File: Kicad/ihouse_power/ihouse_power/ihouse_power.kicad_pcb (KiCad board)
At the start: 2 copper layers, 212 x 156 mm, 203 parts, among them J1 Conn_02x12_Top_Bottom, J10 Conn_02x07_Odd_Even, J11 Conn_01x06, J13 RJ33_Shielded, J14 Optic, J15 Hum1, J16 Hum2, J17 Hum3, J18 Temp, J19 I2C, J2 Conn_02x05_Top_Bottom, J20 Conn_02x05_Top_Bottom, J21 RS232, J22 Nextion, J3 Conn_01x20, J4 Conn_01x20, J5 Conn_01x16, J6 Conn_01x06, J7 Conn_02x07_Odd_Even, J8 Conn_01x16, J9 Conn_01x06, K1 FINDER-34.51, K10 FINDER-34.51, K11 FINDER-34.51, K12 FINDER-34.51, K13 FINDER-34.51, K14 FINDER-41.52, K2 FINDER-34.51, K3 FINDER-34.51, K4 FINDER-34.51, K5 FINDER-34.51, K6 FINDER-34.51, K7 FINDER-34.51, K8 FINDER-34.51, K9 FINDER-34.51, M1 stm32f1_module, M2 tb387_uart_expander, M3 ev1527receiver_module, Q1 IRF7403, Q2 IRF7403, Q3 IRF7403, Q4 IRF7403, Q5 BC847, U1 ULN2004, U10 MAX232, U11 L7805, U12 MAX232, U2 ULN2004, U3 L293D, U4 MCP23017_SO, U5 L7805, U6 EL814, U7 EL814, U8 EL814, U9 24LC32

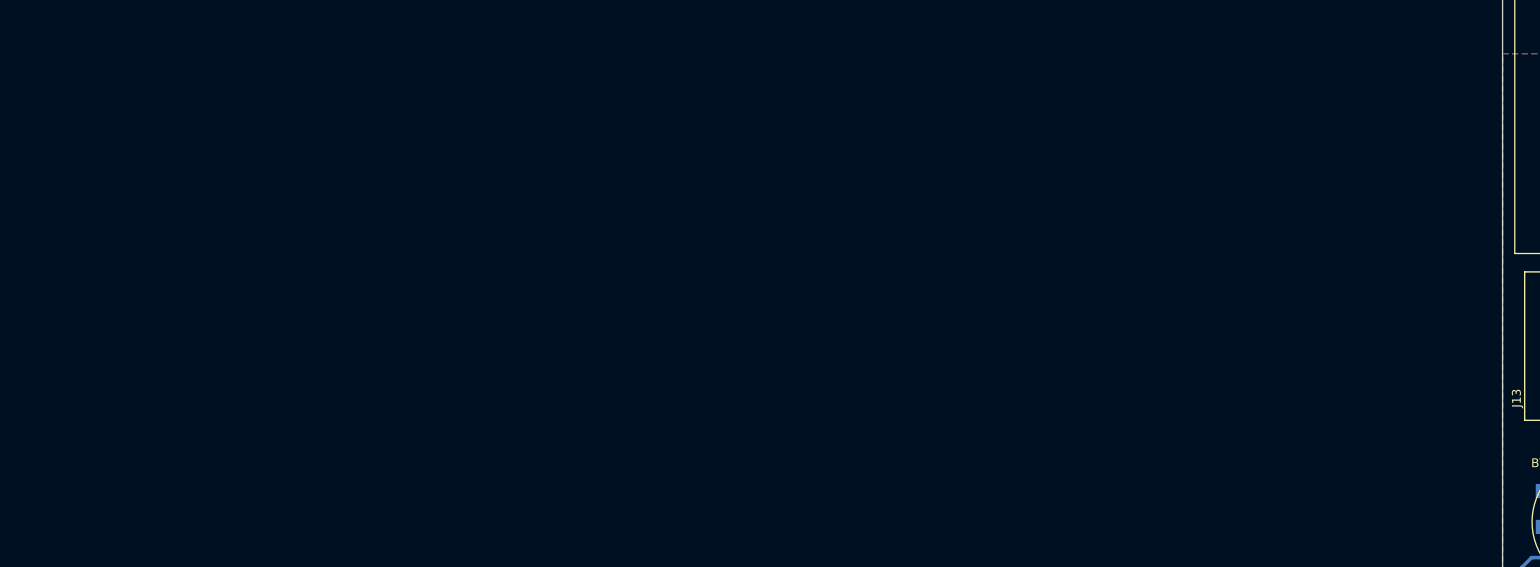
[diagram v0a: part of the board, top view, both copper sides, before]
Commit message: nupiesta paskirstymo dezutes schema ir pcb
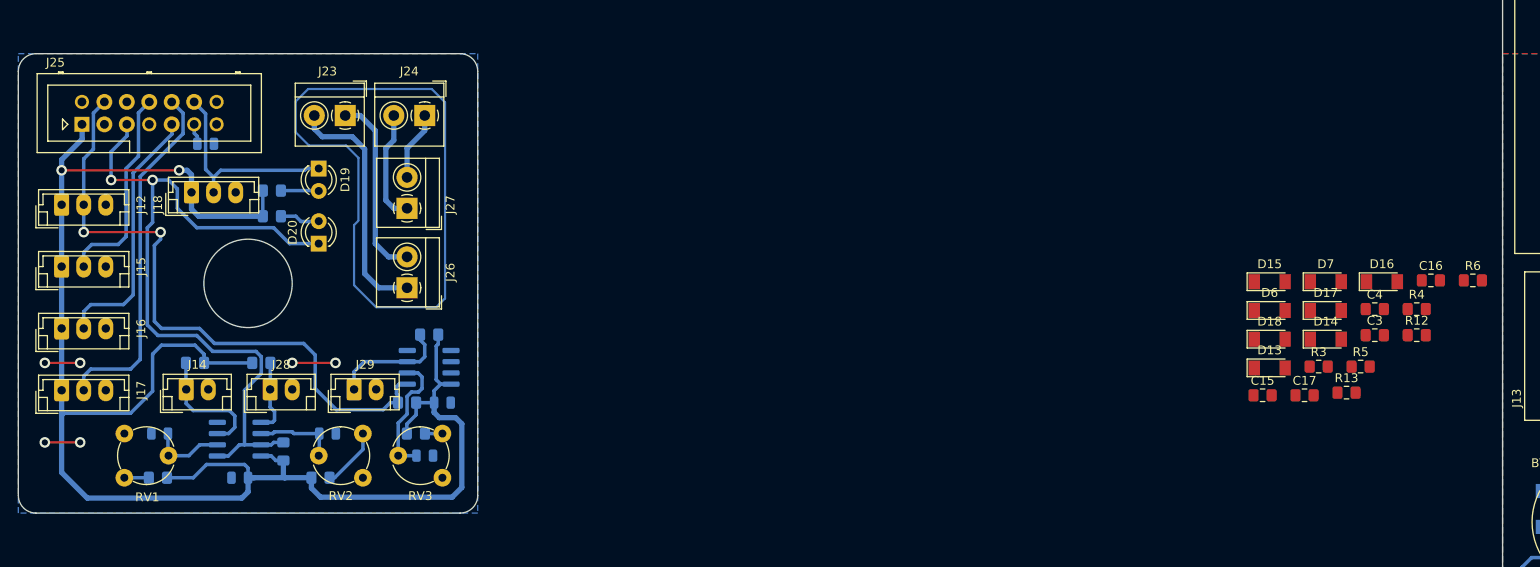
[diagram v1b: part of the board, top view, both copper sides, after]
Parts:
- added C15: 0.1, Capacitor_SMD:C_0805_2012Metric_Pad1.15x1.40mm_HandSolder, F.Cu at (19.8, 94.7)
- added C16: 0.1, Capacitor_SMD:C_0805_2012Metric_Pad1.15x1.40mm_HandSolder, F.Cu at (38.9, 81.7)
- added C17: 0.1, Capacitor_SMD:C_0805_2012Metric_Pad1.15x1.40mm_HandSolder, F.Cu at (24.6, 94.7)
- added C21: 0.1, Capacitor_SMD:C_0805_2012Metric, B.Cu at (-95.9, 104.0)
- added C3: 0.1, Capacitor_SMD:C_0805_2012Metric_Pad1.15x1.40mm_HandSolder, F.Cu at (32.5, 87.9)
- added C35: 0.1, Capacitor_SMD:C_0805_2012Metric, B.Cu at (-105.0, 99.0)
- added C36: 0.1, Capacitor_SMD:C_0805_2012Metric, B.Cu at (-86.0, 99.0)
- added C37: 0.1, Capacitor_SMD:C_0805_2012Metric, B.Cu at (-73.0, 95.5)
- added C38: 0.1, Capacitor_SMD:C_0805_2012Metric, B.Cu at (-75.0, 101.5)
- added C4: 0.1, Capacitor_SMD:C_0805_2012Metric_Pad1.15x1.40mm_HandSolder, F.Cu at (32.5, 84.9)
- added D13: BAS32, Diode_SMD:D_MiniMELF, F.Cu at (20.6, 91.6)
- added D14: BAS32, Diode_SMD:D_MiniMELF, F.Cu at (27.0, 88.3)
- added D15: BAS32, Diode_SMD:D_MiniMELF, F.Cu at (20.6, 81.8)
- added D16: BAS32, Diode_SMD:D_MiniMELF, F.Cu at (33.3, 81.8)
- added D17: BAS85, Diode_SMD:D_MiniMELF, F.Cu at (27.0, 85.1)
- added D18: D, Diode_SMD:D_MiniMELF, F.Cu at (20.6, 88.3)
- added D19: DTH LINK, LED_THT:LED_D3.0mm, F.Cu at (-87.0, 69.0)
- added D20: PHOTO, LED_THT:LED_D3.0mm, F.Cu at (-87.0, 77.5)
- added D6: BAS32, Diode_SMD:D_MiniMELF, F.Cu at (20.6, 85.1)
- added D7: BAS32, Diode_SMD:D_MiniMELF, F.Cu at (27.0, 81.8)
- added J12: OPTIC, Connector_JST:JST_EH_B3B-EH-A_1x03_P2.50mm_Vertical, F.Cu at (-116.1, 73.1)
- added J14: OPT1, Connector_JST:JST_EH_B2B-EH-A_1x02_P2.50mm_Vertical, F.Cu at (-102.0, 94.0)
- added J15: LEAK1, Connector_JST:JST_EH_B3B-EH-A_1x03_P2.50mm_Vertical, F.Cu at (-116.1, 80.1)
- added J16: LEAK2, Connector_JST:JST_EH_B3B-EH-A_1x03_P2.50mm_Vertical, F.Cu at (-116.1, 87.1)
- added J17: LEAK3, Connector_JST:JST_EH_B3B-EH-A_1x03_P2.50mm_Vertical, F.Cu at (-116.1, 94.1)
- added J18: DHT22, Connector_JST:JST_EH_B3B-EH-A_1x03_P2.50mm_Vertical, F.Cu at (-101.4, 71.7)
- added J23: Valve1, TerminalBlock_4Ucon:TerminalBlock_4Ucon_1x02_P3.50mm_Horizontal, F.Cu at (-84.0, 63.0)
- added J24: Valve2, TerminalBlock_4Ucon:TerminalBlock_4Ucon_1x02_P3.50mm_Horizontal, F.Cu at (-75.0, 63.0)
- added J25: Conn_01x14, Connector_Multicomp:Multicomp_MC9A12-1434_2x07_P2.54mm_Vertical, F.Cu at (-113.8, 64.0)
- added J26: Valve1, TerminalBlock_4Ucon:TerminalBlock_4Ucon_1x02_P3.50mm_Horizontal, F.Cu at (-77.0, 82.5)
- added J27: Valve2, TerminalBlock_4Ucon:TerminalBlock_4Ucon_1x02_P3.50mm_Horizontal, F.Cu at (-77.0, 73.5)
- added J28: OPT2, Connector_JST:JST_EH_B2B-EH-A_1x02_P2.50mm_Vertical, F.Cu at (-92.5, 94.0)
- added J29: OPT3, Connector_JST:JST_EH_B2B-EH-A_1x02_P2.50mm_Vertical, F.Cu at (-83.0, 94.0)
- added R12: 100, Resistor_SMD:R_0805_2012Metric_Pad1.15x1.40mm_HandSolder, F.Cu at (37.3, 87.9)
- added R13: 47k, Resistor_SMD:R_0805_2012Metric_Pad1.15x1.40mm_HandSolder, F.Cu at (29.3, 94.4)
- added R14: 4.7k, Resistor_SMD:R_0805_2012Metric_Pad1.15x1.40mm_HandSolder, B.Cu at (-92.3, 71.5)
- added R15: R, Resistor_SMD:R_0805_2012Metric_Pad1.15x1.40mm_HandSolder, B.Cu at (-101.0, 91.0)
- added R17: 100, Resistor_SMD:R_0805_2012Metric_Pad1.15x1.40mm_HandSolder, B.Cu at (-105.2, 104.0)
- added R18: R, Resistor_SMD:R_0805_2012Metric_Pad1.15x1.40mm_HandSolder, B.Cu at (-93.5, 91.0)
- added R19: 100, Resistor_SMD:R_0805_2012Metric_Pad1.15x1.40mm_HandSolder, B.Cu at (-86.8, 104.0)
- added R20: 4.7k, Resistor_SMD:R_0805_2012Metric_Pad1.15x1.40mm_HandSolder, B.Cu at (-92.3, 74.4)
- added R24: R, Resistor_SMD:R_0805_2012Metric_Pad1.15x1.40mm_HandSolder, B.Cu at (-74.5, 87.8)
- added R25: 10k, Resistor_SMD:R_0805_2012Metric_Pad1.15x1.40mm_HandSolder, B.Cu at (-91.0, 101.0)
- added R26: 100, Resistor_SMD:R_0805_2012Metric_Pad1.15x1.40mm_HandSolder, B.Cu at (-76.0, 99.0)
- added R27: 10k, Resistor_SMD:R_0805_2012Metric_Pad1.15x1.40mm_HandSolder, B.Cu at (-77.0, 95.5)
- added R3: 100, Resistor_SMD:R_0805_2012Metric_Pad1.15x1.40mm_HandSolder, F.Cu at (26.2, 91.4)
- added R4: 100, Resistor_SMD:R_0805_2012Metric_Pad1.15x1.40mm_HandSolder, F.Cu at (37.3, 84.9)
- added R5: 100, Resistor_SMD:R_0805_2012Metric_Pad1.15x1.40mm_HandSolder, F.Cu at (30.9, 91.4)
- added R6: 100, Resistor_SMD:R_0805_2012Metric_Pad1.15x1.40mm_HandSolder, F.Cu at (43.6, 81.7)
- added REF**: R_0805_2012Metric, Resistor_SMD:R_0805_2012Metric, B.Cu at (-99.8, 66.2)
- added RV1: 5k, Potentiometer_THT:Potentiometer_Piher_PT-6-V_Vertical, F.Cu at (-109.0, 104.0)
- added RV2: 5k, Potentiometer_THT:Potentiometer_Piher_PT-6-V_Vertical, F.Cu at (-82.0, 99.0)
- added RV3: 5k, Potentiometer_THT:Potentiometer_Piher_PT-6-V_Vertical, F.Cu at (-73.0, 99.0)
- added U6: LM393, Package_SO:SOIC-8_3.9x4.9mm_P1.27mm, B.Cu at (-96.0, 99.6)
- added U7: LM393, Package_SO:SOIC-8_3.9x4.9mm_P1.27mm, B.Cu at (-74.5, 91.5)
- C12, C13, C14, C18, C19, C20: value C -> 0.1
- D10: value D -> BAS32
- R31: value 100 -> 47R
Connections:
- net /MCU plokste/A15 renamed /MCU plokste/PA15
- net /MCU plokste/A2 renamed /MCU plokste/PA2
- net /MCU plokste/A3 renamed /MCU plokste/PA3
- net /MCU plokste/A8 renamed /MCU plokste/PA8
- net /MCU plokste/C13 renamed /MCU plokste/PC13
- net /MCU plokste/C14 renamed /MCU plokste/PC14
- net /MCU plokste/C15 renamed /MCU plokste/PC15
- C12 pad 1: /MCU plokste/VDDA -> /MCU plokste/5VDDA
- C14 pad 1: /MCU plokste/OPTIC_AI -> /MCU plokste/PA6
- C18 pad 1: /MCU plokste/VDDA -> /MCU plokste/5VDDA
- C19 pad 1: /MCU plokste/VDDA -> /MCU plokste/5VDDA
- C20 pad 1: /MCU plokste/VDDA -> /MCU plokste/5VDDA
- C27 pad 1: /MCU plokste/A7 -> /MCU plokste/PA0
- C5 pad 1: /MCU plokste/LPULSE -> /MCU plokste/PB3
- D10 pad 2: /MCU plokste/A7 -> /MCU plokste/PA0
- J1 pad 11: /K2.11 -> /Reliu modulis/K2.11
- J1 pad 12: /K1.11 -> /Reliu modulis/K1.11
- J1 pad 23: /K2.14 -> /Reliu modulis/K2.14
- J1 pad 24: /K1.14 -> /Reliu modulis/K1.14
- J3 pad 10: /MCU plokste/LPULSE -> /MCU plokste/PB3
- J4 pad 10: /MCU plokste/A5 -> /MCU plokste/PA5
- J4 pad 11: /MCU plokste/A6 -> /MCU plokste/PA6
- J4 pad 12: /MCU plokste/A7 -> /MCU plokste/PA7
- J4 pad 15: /MCU plokste/LPULSE1 -> /MCU plokste/PB10
- J4 pad 16: /MCU plokste/LPULSE2 -> /MCU plokste/PB11
- J4 pad 5: /MCU plokste/A0 -> /MCU plokste/PA0
- J4 pad 6: /MCU plokste/A1 -> /MCU plokste/PA1
- J4 pad 9: /MCU plokste/A4 -> /MCU plokste/PA4
- K1 pad 11: /K1.11 -> /Reliu modulis/K1.11
- K1 pad 14: /K1.14 -> /Reliu modulis/K1.14
- K2 pad 11: /K2.11 -> /Reliu modulis/K2.11
- K2 pad 14: /K2.14 -> /Reliu modulis/K2.14
- M1 pad 10: /MCU plokste/HUM3_AI -> /MCU plokste/PA5
- M1 pad 11: /MCU plokste/TEMP_AI -> /MCU plokste/PA6
- M1 pad 12: /MCU plokste/A7 -> /MCU plokste/PA7
- M1 pad 15: /MCU plokste/LPULSE1 -> /MCU plokste/PB10
- M1 pad 16: /MCU plokste/LPULSE2 -> /MCU plokste/PB11
- M1 pad 30: /MCU plokste/LPULSE -> /MCU plokste/PB3
- M1 pad 5: /MCU plokste/OPTIC_AI -> /MCU plokste/PA0
- M1 pad 6: /MCU plokste/HUM1_AI -> /MCU plokste/PA1
- M1 pad 9: /MCU plokste/HUM2_AI -> /MCU plokste/PA4
- R10 pad 2: /MCU plokste/A7 -> /MCU plokste/PA0
- R11 pad 1: /MCU plokste/A7 -> /MCU plokste/PA0
- R2 pad 1: /MCU plokste/LPULSE -> Net-(D17-Pad2)
- R2 pad 2: /MCU plokste/5VDC -> /MCU plokste/3VDC
- R23 pad 1: /MCU plokste/OPTIC_AI -> /MCU plokste/PA6
- R23 pad 2: /MCU plokste/Optic -> /MCU plokste/OPTIC
- R31 pad 2: /MCU plokste/VDDA -> /MCU plokste/5VDDA
- R36 pad 1: /MCU plokste/230N -> /MCU plokste/230L
- R37 pad 1: /MCU plokste/230L -> /MCU plokste/230N
- U8 pad 4: /MCU plokste/LPULSE -> Net-(D17-Pad2)
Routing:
- net /Paskirstymo dezute/5VDC: track 0.00 -> 193.8 mm, vias 0 -> 2
- net /Paskirstymo dezute/OPTICWC: track 0.00 -> 84.7 mm, vias 0 -> 2
- net Net-(J507-Pad11): track 0.00 -> 78.4 mm
- net /Paskirstymo dezute/OPTIC: track 0.00 -> 72.3 mm, vias 0 -> 2
- net Net-(J17-Pad2): track 0.00 -> 40.5 mm
- net Net-(J16-Pad2): track 0.00 -> 29.4 mm
- net Net-(J23-Pad2): track 0.00 -> 27.7 mm
- net Net-(J15-Pad2): track 0.00 -> 23.5 mm
- net /Paskirstymo dezute/DATA: track 0.00 -> 23.5 mm
- net Net-(J23-Pad1): track 0.00 -> 21.1 mm
- net /Paskirstymo dezute/COM: track 0.00 -> 15.2 mm, vias 0 -> 6
- net Net-(C38-Pad1): track 0.00 -> 14.4 mm
- net Net-(J14-Pad1): track 0.00 -> 14.3 mm
- net Net-(J29-Pad1): track 0.00 -> 13.4 mm
- net Net-(J24-Pad2): track 0.00 -> 12.7 mm
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- added copper zone on B.Cu, net /Paskirstymo dezute/COM
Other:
- board size 212 x 156 mm -> 380 x 156 mm
- net class Power added: clearance 0.3, trace_width 0.25, via_dia 0.8, via_drill 0.4

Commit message: schemos korekcijos ir ploksciu paruosimas
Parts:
- removed 1, 2, 3, 4: SolderWirePad_1x01_Drill0.8mm, Connector_Wire:SolderWirePad_1x01_Drill0.8mm
- removed the ? at (85.4, 60.1)
- removed the ? at (72.1, 60.1)
- removed the ? at (58.9, 60.1)
- removed the ? at (103.8, 105.7)
- removed the C3 at (69.2, 59.6)
- removed the C4 at (56.2, 59.6)
- removed the D6 at (77.7, 45.7)
- removed the D7 at (64.6, 45.7)
- removed J11: Conn_01x06, Connector_Molex:Molex_KK-254_AE-6410-06A_1x06_P2.54mm_Vertical
- removed M1: stm32f1_module, stm32f1_module:stm32f1_module
- removed the R12 at (72.9, 39.3)
- removed the R13 at (81.6, 39.3)
- removed the R14 at (72.9, 49.5)
- removed the R15 at (59.7, 49.5)
- removed the R17 at (72.9, 44.4)
- removed the R18 at (81.6, 44.4)
- removed the R19 at (59.7, 44.4)
- removed the R20 at (68.4, 44.4)
- removed the R3 at (58.9, 57.0)
- removed the R4 at (72.1, 57.0)
- removed the R5 at (81.6, 49.5)
- removed the R6 at (68.4, 49.5)
- removed the U6 at (76.0, 50.4)
- removed the U7 at (63.0, 50.4)
- added C39: C, Capacitor_SMD:C_0805_2012Metric_Pad1.15x1.40mm_HandSolder, B.Cu at (-89.3, 155.0)
- added C40: 0.1, Capacitor_SMD:C_0805_2012Metric_Pad1.15x1.40mm_HandSolder, F.Cu at (42.7, 121.9)
- added C41: 0.1, Capacitor_SMD:C_0805_2012Metric, B.Cu at (-150.5, 153.0)
- added C42: 0.1, Capacitor_SMD:C_0805_2012Metric, B.Cu at (-147.4, 147.4)
- added CN6: Conn_01x06, Connector_PinHeader_2.54mm:PinHeader_1x06_P2.54mm_Vertical, B.Cu at (-95.0, 150.0)
- added D21: BAS85, Diode_SMD:D_MiniMELF, F.Cu at (19.0, 76.0)
- added D22: BAS32, Diode_SMD:D_MiniMELF, F.Cu at (28.6, 21.5)
- added J31: Conn_01x01, Connector_PinHeader_2.54mm:PinHeader_1x01_P2.54mm_Vertical, F.Cu at (112.0, 113.0)
- added J31: Conn_01x06, Connector_PinHeader_2.54mm:PinHeader_1x06_P2.54mm_Vertical, F.Cu at (23.1, 22.2)
- added J32: Conn_01x06, Connector_PinHeader_2.54mm:PinHeader_1x06_P2.54mm_Vertical, B.Cu at (-78.3, 150.0)
- added R28: 4.7k, Resistor_SMD:R_0805_2012Metric, B.Cu at (-50.9, 155.0)
- added R29: 4.7k, Resistor_SMD:R_0805_2012Metric_Pad1.15x1.40mm_HandSolder, B.Cu at (37.3, 119.5)
- added R30: 4.7k, Resistor_SMD:R_0805_2012Metric, B.Cu at (-97.5, 154.0)
- added R32: R_PHOTO, Resistor_THT:R_Axial_DIN0204_L3.6mm_D1.6mm_P5.08mm_Horizontal, F.Cu at (-117.0, 146.8)
- added R33: R, Resistor_SMD:R_0805_2012Metric_Pad1.15x1.40mm_HandSolder, B.Cu at (-148.2, 152.9)
- added R49: 10k, Resistor_SMD:R_0805_2012Metric_Pad1.15x1.40mm_HandSolder, F.Cu at (-145.0, 103.8)
- added R50: 1k, Resistor_SMD:R_0805_2012Metric_Pad1.15x1.40mm_HandSolder, F.Cu at (34.2, 21.4)
- added REF**: MountingHole_3.2mm_M3, MountingHole:MountingHole_3.2mm_M3, F.Cu at (-128.0, 150.0)
- added REF**: MountingHole_3.2mm_M3, MountingHole:MountingHole_3.2mm_M3, F.Cu at (-72.0, 150.0)
- added RV4: 5k, Potentiometer_THT:Potentiometer_Piher_PT-6-V_Vertical, F.Cu at (-139.1, 146.8)
- added SW1: BLDR, Resistor_THT:R_Axial_DIN0411_L9.9mm_D3.6mm_P15.24mm_Horizontal, B.Cu at (-63.0, 155.0)
- added SW2: USER, Resistor_THT:R_Axial_DIN0411_L9.9mm_D3.6mm_P15.24mm_Horizontal, B.Cu at (-108.0, 155.0)
- added SW3: RESET, Resistor_THT:R_Axial_DIN0411_L9.9mm_D3.6mm_P15.24mm_Horizontal, B.Cu at (-153.2, 155.0)
- added U13: LM393, Package_SO:SOIC-8_3.9x4.9mm_P1.27mm, B.Cu at (-153.0, 148.6)
- BT1: value 3V3 -> 3V0
- C5, D8, R16, R2, R21, R22, R36, R37, R7, U8: moved to F.Cu
- D18: value D -> BAS32
- R34: value 22k -> 100; footprint Resistor_SMD:R_1206_3216Metric -> Resistor_SMD:R_0805_2012Metric_Pad1.15x1.40mm_HandSolder
- R35: value 22k -> 10k; footprint Resistor_SMD:R_1206_3216Metric -> Resistor_SMD:R_0805_2012Metric_Pad1.15x1.40mm_HandSolder
- moved R35 243.0 mm to (-146.4, 152.9), turned to 90 degrees
- moved R34 231.9 mm to (-142.4, 153.9), turned to 0 degrees
- moved C31 206.8 mm to (-136.2, 109.3)
- moved C32 206.8 mm to (-136.2, 104.4)
- moved C33 206.8 mm to (-126.9, 96.0)
- moved C34 206.8 mm to (-136.2, 100.4)
- moved J21 206.8 mm to (-142.0, 111.4)
- moved J22 206.8 mm to (-121.2, 99.3)
- moved U12 206.8 mm to (-128.0, 103.5)
- moved R48 167.3 mm to (-66.2, 148.8)
- moved D12 167.3 mm to (-63.6, 148.8), turned to 90 degrees
- moved Q5 161.6 mm to (-57.6, 148.7)
- moved ? 161.1 mm to (-60.9, 150.6)
- moved ? 160.6 mm to (-60.9, 147.1)
- moved R47 160.4 mm to (-54.1, 148.8), turned to 90 degrees
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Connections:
- net /COM renamed Net-(C31-Pad1)
- net /MCP23017 modulis/SCK renamed /MCP23017 modulis/SCL
- net /RS1 renamed /RSRX
- net /RS2 renamed /RSTX
- BT1 pad 1: /MCU plokste/VBAT -> Net-(BT1-Pad1)
- D16 pad 2: /MCU plokste/DHTIO_PIN -> /MCU plokste/PC13
- J13 pad 4: /MCU plokste/RCEN -> Net-(J13-Pad4)
- J14 pad 1: /MCU plokste/VDDA -> /MCU plokste/5VDDA
- J15 pad 1: /MCU plokste/VDDA -> /MCU plokste/5VDDA
- J16 pad 1: /MCU plokste/VDDA -> /MCU plokste/5VDDA
- J17 pad 1: /MCU plokste/VDDA -> /MCU plokste/5VDDA
- J18 pad 1: /MCU plokste/VDDA -> /MCU plokste/5VDDA
- J19 pad 2: /MCU plokste/SCK -> /MCU plokste/SCL
- J21 pad 4: /RCEN -> Net-(J21-Pad4)
- J3 pad 12: /MCU plokste/QCH_D2 -> /MCU plokste/PA12
- J3 pad 13: /MCU plokste/QCH_D3 -> /MCU plokste/PA11
- J3 pad 4: /MCU plokste/QCH_D1 -> /MCU plokste/PB9
- J3 pad 5: /MCU plokste/QCH_D0 -> /MCU plokste/PB8
- J3 pad 7: /MCU plokste/SCK -> /MCU plokste/SCL
- J3 pad 8: /MCU plokste/PWM4 -> /MCU plokste/PWM2
- J3 pad 9: /MCU plokste/PWM3 -> /MCU plokste/PWM1
- J4 pad 13: /MCU plokste/PWM1 -> /MCU plokste/PWM3
- J4 pad 14: /MCU plokste/PWM2 -> /MCU plokste/PWM4
- J7 pad 3: /MCU plokste/SCK -> /MCU plokste/SCL
- Q5 pad 2: /MCU plokste/COM1 -> /MCU plokste/COM@1
- R12 pad 1: /MCU plokste/DHTIO_PIN -> /MCU plokste/PC13
- R34 pad 1: /MCU plokste/K2.14 -> /MCU plokste/5V@1
- R35 pad 1: /MCU plokste/K2.11 -> /MCU plokste/5V@1
- R46 pad 2: /MCU plokste/BUZZ -> Net-(J32-Pad1)
- R47 pad 1: /MCU plokste/COM1 -> /MCU plokste/COM@1
- R48 pad 1: /MCU plokste/12VDC -> /MCU plokste/BUZPL
- R48 pad 2: /MCU plokste/BUZPL -> /MCU plokste/5V@1
- R9 pad 2: /MCU plokste/SCK -> /MCU plokste/SCL
- U10 pad 11: /MCU plokste/NEXRX -> /MCU plokste/PA2
- U10 pad 12: /MCU plokste/NEXTX -> /MCU plokste/PA3
- U10 pad 8: /MCU plokste/RCEN -> Net-(U10-Pad8)
- U10 pad 9: /MCU plokste/RCEN -> Net-(U10-Pad9)
- U12 pad 7: /RCEN -> Net-(U12-Pad7)
- U9 pad 6: /MCU plokste/SCK -> /MCU plokste/SCL
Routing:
- net /MCU plokste/5V@1: track 0.00 -> 107.0 mm
- net /MCU plokste/VDDA: track 81.8 -> 0.00 mm
- net /MCU plokste/5VDDA: track 0.00 -> 81.8 mm
- net Net-(J32-Pad4): track 2.31 -> 75.9 mm, vias 0 -> 2
- net Net-(J32-Pad2): track 0.00 -> 65.7 mm
- net Net-(CN6-Pad3): track 0.00 -> 61.4 mm
- net /MCU plokste/5VDC: track 231.2 -> 183.4 mm, vias 6 -> 5
- net /MCU plokste/PA3: track 0.00 -> 46.3 mm
- net /MCU plokste/NEXTX: track 46.3 -> 0.00 mm
- net /MCU plokste/A7: track 42.1 -> 0.00 mm
- net /MCU plokste/3V@1: track 0.00 -> 40.8 mm
- net Net-(R32-Pad2): track 0.00 -> 39.5 mm
- net /MCU plokste/TEMP_AI: track 35.5 -> 0.00 mm
- net /MCU plokste/PA2: track 0.00 -> 33.6 mm
- net /MCU plokste/NEXRX: track 33.6 -> 0.00 mm
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- added copper zone on B.Cu, net /MCU plokste/COM@1
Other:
- board size 380 x 156 mm -> 419 x 136 mm

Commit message: schemos ir pcb ruosimas
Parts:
- removed 0R: R_0805_2012Metric_Pad1.15x1.40mm_HandSolder, Resistor_SMD:R_0805_2012Metric_Pad1.15x1.40mm_HandSolder
- removed 0R: 0R, Resistor_SMD:R_0805_2012Metric_Pad1.15x1.40mm_HandSolder
- removed BT1: 3V0, 1220 Battery Holder:Battery_holder_1220
- removed the C15 at (77.8, 122.8)
- removed the C15 at (19.8, 94.7)
- removed the C16 at (90.3, 122.8)
- removed the C16 at (38.9, 81.7)
- removed the C17 at (102.8, 122.8)
- removed the C17 at (24.6, 94.7)
- removed C18, C19, C20: 0.1, Capacitor_SMD:C_0805_2012Metric_Pad1.15x1.40mm_HandSolder
- removed the C21 at (115.4, 122.9)
- removed the C21 at (-67.9, 128.0)
- removed C37, C38: 0.1, Capacitor_SMD:C_0805_2012Metric
- removed J12: OPTIC, Connector_JST:JST_EH_B3B-EH-A_1x03_P2.50mm_Vertical
- removed J13: RJ33_Shielded, rj45_vertical_shelded:RJ45_Vertical
- removed the J14 at (65.2, 126.3)
- removed the J15 at (77.8, 126.3)
- removed the J16 at (90.3, 126.3)
- removed the J17 at (102.8, 126.3)
- removed the J18 at (115.3, 126.4)
- removed J29: OPT3, Connector_JST:JST_EH_B2B-EH-A_1x02_P2.50mm_Vertical
- removed the J31 at (112.0, 113.0)
- removed the J31 at (23.1, 22.2)
- removed M3: ev1527receiver_module, ev1527:EV1527_Receiver
- removed R16, R21, R22, R36, R37: 22k, Resistor_SMD:R_1206_3216Metric
- removed R24, R26 (x2): 100, Resistor_SMD:R_0805_2012Metric_Pad1.15x1.40mm_HandSolder
- removed R24: R, Resistor_SMD:R_0805_2012Metric_Pad1.15x1.40mm_HandSolder
- removed the R25 at (92.8, 122.8)
- removed R27, R29 (x2): 4.7k, Resistor_SMD:R_0805_2012Metric_Pad1.15x1.40mm_HandSolder
- removed R27: 10k, Resistor_SMD:R_0805_2012Metric_Pad1.15x1.40mm_HandSolder
- removed the R28 at (82.8, 122.8)
- removed the R30 at (107.8, 122.8)
- removed the R32 at (117.8, 122.9)
- removed the R33 at (120.2, 122.9)
- removed the REF** at (124.0, 71.0)
- removed the REF** at (133.0, 60.0)
- removed the REF** at (105.0, 62.0)
- removed the REF** at (124.7, 61.7)
- removed the REF** at (122.1, 61.7)
- removed the REF** at (111.7, 61.7)
- removed the REF** at (109.1, 61.7)
- removed the REF** at (66.0, 101.0)
- removed the REF** at (111.8, 67.8)
- removed the REF** at (109.0, 77.0)
- removed the REF** at (67.0, 116.0)
- removed the REF** at (57.0, 124.0)
- removed the REF** at (91.0, 106.0)
- removed the REF** at (132.0, 26.0)
- removed the REF** at (52.0, 26.0)
- removed the REF** at (52.0, 126.0)
- removed the REF** at (128.0, 126.0)
- removed the REF** at (-71.8, 90.2)
- removed the REF** at (123.0, 108.0)
- removed the REF** at (87.3, 119.5)
- removed the REF** at (53.0, 101.0)
- removed the REF** at (66.0, 108.0)
- removed the REF** at (66.0, 77.0)
- removed the REF** at (92.0, 77.0)
- removed RV3: 5k, Potentiometer_THT:Potentiometer_Piher_PT-6-V_Vertical
- removed TH4: Thermistor_PTC, Resistor_SMD:R_1206_3216Metric_Pad1.42x1.75mm_HandSolder
- removed U7: LM393, Package_SO:SOIC-8_3.9x4.9mm_P1.27mm
- removed U8: EL814, Package_DIP:DIP-4_W7.62mm_LongPads
- added C15: 0.1, Capacitor_SMD:C_0805_2012Metric_Pad1.15x1.40mm_HandSolder, F.Cu at (123.9, -54.0)
- added C16: 0.1, Capacitor_SMD:C_0805_2012Metric_Pad1.15x1.40mm_HandSolder, F.Cu at (118.1, -44.8)
- added C17: 0.1, Capacitor_SMD:C_0805_2012Metric_Pad1.15x1.40mm_HandSolder, F.Cu at (126.5, -51.1)
- added C21: 0.1, Capacitor_SMD:C_0805_2012Metric, B.Cu at (116.2, 162.0)
- added J31: Conn_01x06, Connector_PinHeader_2.54mm:PinHeader_1x06_P2.54mm_Vertical, F.Cu at (107.0, -91.4)
- added JP5: 0R, Resistor_SMD:R_0805_2012Metric_Pad1.15x1.40mm_HandSolder, B.Cu at (96.1, 148.8)
- added JP5: 0R, Resistor_SMD:R_0805_2012Metric_Pad1.15x1.40mm_HandSolder, B.Cu at (96.1, 157.8)
- C12: value 0.1 -> 10,0; footprint Capacitor_SMD:C_0805_2012Metric_Pad1.15x1.40mm_HandSolder -> Capacitor_SMD:CP_Elec_4x4.5; moved to F.Cu
- C13, C14, C27, C6, C7, C8, C9, D10, D4, D5, D9, Q1, Q2, Q3, Q4, R10, R11, R23, R31, R38, R39, R40, R41, R42, R43, R44, R45, R8, R9, SW1, SW2, SW3, TH2, U10, U11, U9: moved to F.Cu
- C23, C24, C25: value C -> 0.1; moved to F.Cu
- C26: value CP -> 100x16V
- C5: value 1.0 -> 10n; footprint Capacitor_SMD:C_1206_3216Metric_Pad1.42x1.75mm_HandSolder -> Capacitor_SMD:C_0805_2012Metric
- D17: value BAS85 -> BAS32
- D8: value D -> POWER; footprint Diode_SMD:D_MiniMELF -> LED_THT:LED_D3.0mm
- F3, F4, F5, F6: footprint Resistor_THT:R_Axial_DIN0204_L3.6mm_D1.6mm_P5.08mm_Horizontal -> Fuse:Fuse_2920_7451Metric_Pad2.10x5.45mm_HandSolder
- J19: footprint Connector_JST:JST_XH_B04B-XH-A_1x04_P2.50mm_Vertical -> Connector_JST:JST_PH_B4B-PH-K_1x04_P2.00mm_Vertical
- R13: value 47k -> 10k
- R32: moved to B.Cu
- R48: footprint Resistor_SMD:R_1206_3216Metric -> Resistor_SMD:R_0805_2012Metric
- R7: value 22k -> 4.7k; footprint Resistor_SMD:R_1206_3216Metric -> Resistor_SMD:R_0805_2012Metric; moved to B.Cu
- REF**: value R_1206_3216Metric_Pad1.42x1.75mm_HandSolder -> (none)
- moved J4 210.1 mm to (97.7, -91.4), turned to 0 degrees
- moved C6 210.1 mm to (142.3, -75.3)
- moved R23 209.5 mm to (146.1, -71.4), turned to 0 degrees
- moved R31 201.4 mm to (136.2, -63.6), turned to 0 degrees
- moved R35 197.8 mm to (49.4, 180.9)
- moved D13 197.4 mm to (134.6, -69.6)
- moved R5 196.7 mm to (141.3, -71.4)
- moved D17 196.0 mm to (124.3, -85.1)
- moved J32 193.9 mm to (113.1, 181.4)
- moved ? 192.9 mm to (129.4, 182.0)
- moved ? 192.9 mm to (129.4, 178.5)
- moved C39 192.9 mm to (101.0, 186.4)
- moved C42 192.9 mm to (42.9, 178.8)
- moved CN6 192.9 mm to (95.3, 181.4)
- moved D12 192.9 mm to (126.7, 180.2)
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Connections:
- net /MCU plokste/OPTIC_WC renamed /MCU plokste/OPTICWC
- net /MCU plokste/PB2 renamed Net-(C39-Pad1)
- net Net-(J14-Pad1) renamed /Paskirstymo dezute/OPT1
- net Net-(J23-Pad1) renamed /Paskirstymo dezute/V1A
- net Net-(J23-Pad2) renamed /Paskirstymo dezute/V1B
- net Net-(J24-Pad1) renamed /Paskirstymo dezute/V2A
- net Net-(J24-Pad2) renamed /Paskirstymo dezute/V2B
- net Net-(J28-Pad1) renamed /Paskirstymo dezute/OPT2
- C10 pad 2: /MCU plokste/COM1 -> /MCU plokste/COM
- C11 pad 2: /MCU plokste/COM1 -> /MCU plokste/COM
- C12 pad 1: /MCU plokste/5VDDA -> /5VDC
- C12 pad 2: /MCU plokste/COM1 -> Net-(C12-Pad2)
- C13 pad 1: Net-(C13-Pad1) -> /MCU plokste/5VDDA
- C13 pad 2: /MCU plokste/COM1 -> /MCU plokste/COM
- C14 pad 2: /MCU plokste/COM1 -> /MCU plokste/COM
- C23 pad 2: /MCU plokste/COM1 -> /MCU plokste/COM
- C24 pad 2: /MCU plokste/COM1 -> /MCU plokste/COM
- C25 pad 2: /MCU plokste/COM1 -> /MCU plokste/COM
- C26 pad 2: /MCU plokste/COM1 -> /MCU plokste/COM
- C27 pad 2: /MCU plokste/COM1 -> /MCU plokste/COM
- C28 pad 2: /MCU plokste/COM1 -> /MCU plokste/COM
- C29 pad 2: /MCU plokste/COM1 -> /MCU plokste/COM
- C3 pad 2: /MCU plokste/COM1 -> /MCU plokste/COM
- C30 pad 2: /MCU plokste/COM1 -> /MCU plokste/COM
- C31 pad 1: Net-(C31-Pad1) -> Net-(C12-Pad2)
- C4 pad 2: /MCU plokste/COM1 -> /MCU plokste/COM
- C40 pad 2: /MCU plokste/COM1 -> /MCU plokste/COM
- C5 pad 2: /MCU plokste/COM1 -> /MCU plokste/COM
- C6 pad 1: /MCU plokste/COM1 -> /MCU plokste/COM
- CN6 pad 2: /MCU plokste/3V@1 -> Net-(CN6-Pad2)
- D11 pad 4: /MCU plokste/COM1 -> /MCU plokste/COM
- D17 pad 1: /MCU plokste/PB3 -> /MCU plokste/3VDC
- D17 pad 2: Net-(D17-Pad2) -> /MCU plokste/PB3
- D19 pad 1: /Paskirstymo dezute/DATA -> /Paskirstymo dezute/DHTIO
- D4 pad 2: Net-(D4-Pad2) -> /MCU plokste/LPULSE
- D8 pad 1: Net-(D8-Pad1) -> /Paskirstymo dezute/COM
- J14 pad 2: /Paskirstymo dezute/COM -> Net-(J14-Pad2)
- J15 pad 2: Net-(J15-Pad2) -> /Paskirstymo dezute/LEAK1
- J15 pad 3: /Paskirstymo dezute/COM -> Net-(J15-Pad3)
- J16 pad 2: Net-(J16-Pad2) -> /Paskirstymo dezute/LEAK2
- J16 pad 3: /Paskirstymo dezute/COM -> Net-(J16-Pad3)
- J17 pad 2: Net-(J17-Pad2) -> /Paskirstymo dezute/LEAK3
- J17 pad 3: /Paskirstymo dezute/COM -> Net-(J17-Pad3)
- J18 pad 2: /Paskirstymo dezute/DATA -> /Paskirstymo dezute/DHTIO
- J18 pad 3: /Paskirstymo dezute/COM -> Net-(J18-Pad3)
- J19 pad 4: /MCU plokste/COM1 -> /MCU plokste/COM
- J21 pad 3: Net-(C31-Pad1) -> Net-(C12-Pad2)
- J21 pad 6: Net-(C31-Pad1) -> Net-(C12-Pad2)
- J21 pad 7: Net-(C31-Pad1) -> Net-(C12-Pad2)
- J21 pad 8: Net-(C31-Pad1) -> Net-(C12-Pad2)
- J22 pad 4: Net-(C31-Pad1) -> Net-(C12-Pad2)
- J25 pad 10: Net-(J17-Pad2) -> /Paskirstymo dezute/COM
- J25 pad 11: /Paskirstymo dezute/COM -> /Paskirstymo dezute/OPTICWC
- J25 pad 12: /Paskirstymo dezute/DATA -> /Paskirstymo dezute/COM
- J25 pad 2: /Paskirstymo dezute/COM -> /Paskirstymo dezute/5VDC
- J25 pad 3: Net-(J25-Pad3) -> /Paskirstymo dezute/LEAK1
- J25 pad 4: /Paskirstymo dezute/OPTIC -> Net-(J25-Pad4)
- J25 pad 5: /Paskirstymo dezute/OPTICWC -> /Paskirstymo dezute/LEAK2
- J25 pad 7: /Paskirstymo dezute/COM -> /Paskirstymo dezute/LEAK3
- J25 pad 8: Net-(J15-Pad2) -> Net-(J25-Pad8)
- J25 pad 9: Net-(J16-Pad2) -> /Paskirstymo dezute/DHTIO
- J28 pad 2: /Paskirstymo dezute/COM -> Net-(J28-Pad2)
- J3 pad 2: /MCU plokste/COM1 -> /MCU plokste/COM
- J4 pad 19: /MCU plokste/COM1 -> /MCU plokste/COM
- J7 pad 10: /MCU plokste/COM1 -> /MCU plokste/COM
- J7 pad 9: /MCU plokste/COM1 -> /MCU plokste/COM
- Q1 pad 1: /MCU plokste/COM1 -> /MCU plokste/COM
- Q1 pad 2: /MCU plokste/COM1 -> /MCU plokste/COM
- Q1 pad 3: /MCU plokste/COM1 -> /MCU plokste/COM
- Q2 pad 1: /MCU plokste/COM1 -> /MCU plokste/COM
- Q2 pad 2: /MCU plokste/COM1 -> /MCU plokste/COM
- Q2 pad 3: /MCU plokste/COM1 -> /MCU plokste/COM
- Q3 pad 1: /MCU plokste/COM1 -> /MCU plokste/COM
- Q3 pad 2: /MCU plokste/COM1 -> /MCU plokste/COM
- Q3 pad 3: /MCU plokste/COM1 -> /MCU plokste/COM
- Q4 pad 1: /MCU plokste/COM1 -> /MCU plokste/COM
- Q4 pad 2: /MCU plokste/COM1 -> /MCU plokste/COM
- Q4 pad 3: /MCU plokste/COM1 -> /MCU plokste/COM
- R11 pad 2: /MCU plokste/COM1 -> /MCU plokste/COM
- R13 pad 1: /MCU plokste/COM1 -> /MCU plokste/COM
- R2 pad 1: Net-(D17-Pad2) -> /MCU plokste/LPULSE
- R2 pad 2: /MCU plokste/3VDC -> /MCU plokste/PB3
- R31 pad 1: Net-(C13-Pad1) -> /MCU plokste/5VDC
- R42 pad 1: /MCU plokste/COM1 -> /MCU plokste/COM
- R43 pad 1: /MCU plokste/COM1 -> /MCU plokste/COM
- R44 pad 1: /MCU plokste/COM1 -> /MCU plokste/COM
- R45 pad 1: /MCU plokste/COM1 -> /MCU plokste/COM
- R49 pad 2: Net-(C31-Pad1) -> Net-(C12-Pad2)
- R7 pad 1: Net-(R22-Pad2) -> /Paskirstymo dezute/5VDC
- TH2 pad 1: /MCU plokste/COM1 -> /MCU plokste/COM
- TR1 pad 8: Net-(D4-Pad2) -> /MCU plokste/LPULSE
- U10 pad 15: /MCU plokste/COM1 -> /MCU plokste/COM
- U11 pad 2: /MCU plokste/COM1 -> /MCU plokste/COM
- U12 pad 15: Net-(C31-Pad1) -> Net-(C12-Pad2)
- U9 pad 1: /MCU plokste/COM1 -> /MCU plokste/COM
- U9 pad 2: /MCU plokste/COM1 -> /MCU plokste/COM
- U9 pad 3: /MCU plokste/COM1 -> /MCU plokste/COM
- U9 pad 4: /MCU plokste/COM1 -> /MCU plokste/COM
- U9 pad 7: /MCU plokste/COM1 -> /MCU plokste/COM
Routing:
- net /MCU plokste/5VDC: track 183.4 -> 0.00 mm, vias 5 -> 0
- net /MCU plokste/12VDC: track 172.3 -> 0.00 mm, vias 3 -> 0
- net /MCU plokste/5VDDA: track 81.8 -> 0.00 mm
- net /MCU plokste/SCK: track 77.8 -> 0.00 mm
- net /Paskirstymo dezute/5VDC: track 193.8 -> 117.9 mm
- net /MCU plokste/QCH_D1: track 72.9 -> 0.00 mm, vias 2 -> 0
- net /Paskirstymo dezute/OPTIC: track 72.3 -> 0.00 mm, vias 2 -> 0
- net /MCU plokste/QCH_D0: track 69.9 -> 0.00 mm, vias 2 -> 0
- net /MCU plokste/SDA: track 69.4 -> 0.00 mm
- net /MCU plokste/M23ENA: track 54.0 -> 0.00 mm, vias 2 -> 0
- net /MCU plokste/3VDC: track 52.4 -> 0.00 mm
- net /MCU plokste/PA3: track 46.3 -> 0.00 mm
- net /MCU plokste/QCH_D2: track 45.7 -> 0.00 mm
- net /MCU plokste/M1ENA: track 45.1 -> 0.00 mm, vias 2 -> 0
- net /Paskirstymo dezute/OPTICWC: track 84.7 -> 41.0 mm, vias 2 -> 0
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- added copper zone on F.Cu, net Net-(C12-Pad2)
- removed copper zone on B.Cu, net /MCU plokste/COM1
- removed copper zone on F.Cu, net /MCU plokste/COM1
- removed copper zone on B.Cu, net /MCU plokste/VB
- removed copper zone on F.Cu, net Net-(C31-Pad1)
- removed copper zone on B.Cu, net Net-(F3-Pad2)
- removed copper zone on B.Cu, net Net-(F4-Pad2)
- removed copper zone on B.Cu, net Net-(F5-Pad2)
- removed copper zone on B.Cu, net Net-(F6-Pad2)
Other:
- board size 419 x 136 mm -> 243.5 x 139.6 mm
